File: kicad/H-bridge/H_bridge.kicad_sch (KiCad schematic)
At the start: 40 parts, among them J1 Screw_Terminal_01x03, J2 Conn_Coaxial, J3 2453710000, J4 Screw_Terminal_01x02, Q1 IAUT300N10S5N014ATMA1, Q2 IAUT300N10S5N014ATMA1, Q3 IAUT300N10S5N014ATMA1, Q4 IAUT300N10S5N014ATMA1, U1 LTV-817, U2 PDS1-S15-S15-M, U3 HIP4080A

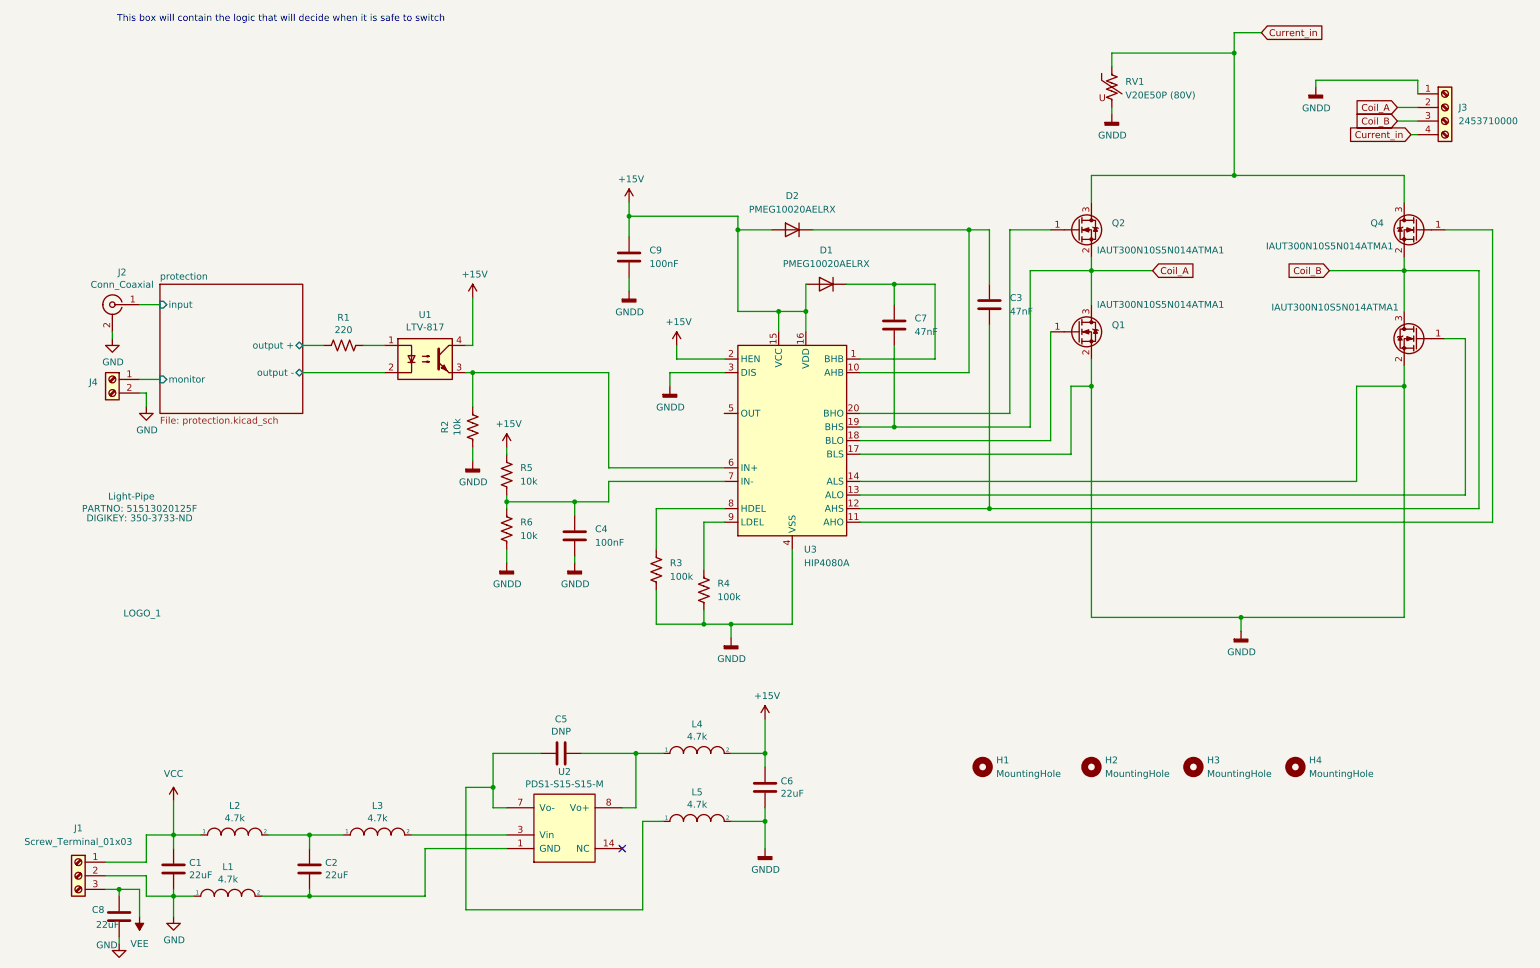
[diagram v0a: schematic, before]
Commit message: Final Board schematics and layouts, Also added custom footprints that were made for the relay and terminal connector block.
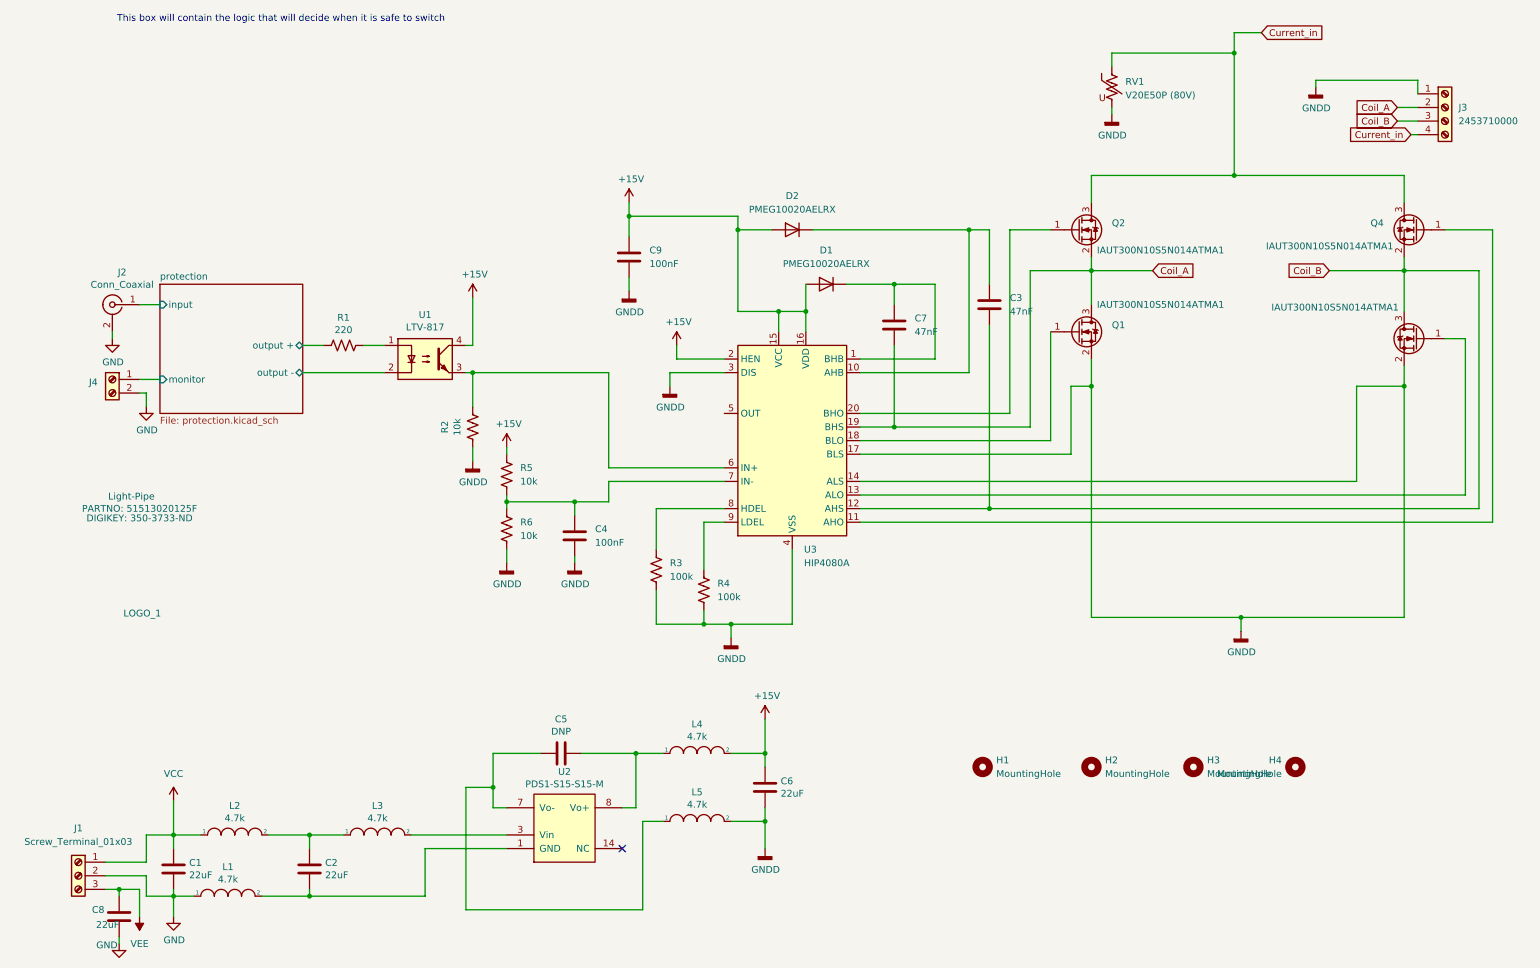
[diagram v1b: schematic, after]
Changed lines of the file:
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@@
 (kicad_sch
-	(version 20231120)
+	(version 20250114)
 	(generator "eeschema")
-	(generator_version "8.0")
+	(generator_version "9.0")
 	(paper "A4")
 	(title_block
@@
 		(date "04/20/2024")
 	)
+	(text "This box will contain the logic that will decide when it is safe to switch"
+		(exclude_from_sim no)
+		(at 51.816 22.86 0)
+		(effects
+			(font
+				(size 1.27 1.27)
+			)
+		)
+	)
 	(junction
 		(at 203.2 91.44)
@@
 		)
 	)
-	(text "This box will contain the logic that will decide when it is safe to switch"
-		(exclude_from_sim no)
-		(at 51.816 22.86 0)
-		(effects
-			(font
-				(size 1.27 1.27)
-			)
-		)
-	)
 	(global_label "Coil_A"
 		(shape input)
@@
 		(lib_id "Mechanical:MountingHole")
 		(at 241.3 162.56 0)
+		(mirror y)
 		(unit 1)
 		(exclude_from_sim yes)
@@
 		(on_board yes)
 		(dnp no)
-		(fields_autoplaced yes)
 		(property "Reference" "H4"
-			(at 243.84 161.2899 0)
+			(at 238.76 161.2899 0)
 			(effects
 				(font
@@
 		)
 		(property "Value" "MountingHole"
-			(at 243.84 163.8299 0)
+			(at 238.76 163.8299 0)
 			(effects
 				(font
@@
 		(at 29.21 72.39)
 		(size 26.67 24.13)
+		(exclude_from_sim no)
+		(in_bom yes)
+		(on_board yes)
+		(dnp no)
 		(fields_autoplaced yes)
 		(stroke
@@
 		)
 	)
+	(embedded_fonts no)
 )
